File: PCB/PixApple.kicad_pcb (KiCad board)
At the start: 2 copper layers, 97.5 x 70 mm, 80 parts, among them J1 USB_C_Receptacle_USB2.0_16P, J10 Conn_01x11, J11 Conn_01x11, J12 Conn_01x02_Pin, J2 Conn_01x02_Pin, J28 Conn_01x01_Pin, J29 Conn_01x01_Pin, J3 Conn_01x01_Pin, J30 Conn_01x01_Pin, J4 Conn_01x01_Pin, J5 Conn_01x05_Pin, J6 Conn_01x02_Pin, J7 Conn_01x01_Pin, J8 Conn_02x03_Odd_Even, J9 Conn_01x04_Pin, M3 MountingHole_3.2mm_M3, SW1 SW_Push, SW2 SW_Push, U1 RP2040, U2 NCP1117-3.3_TO252, U3 W25Q128JVS, U4 SN65HVD230DR, U5 MCP2515-xSO, Y1 ABM8-272-T3, Y2 ABM8-16.000MHZ-B2-T

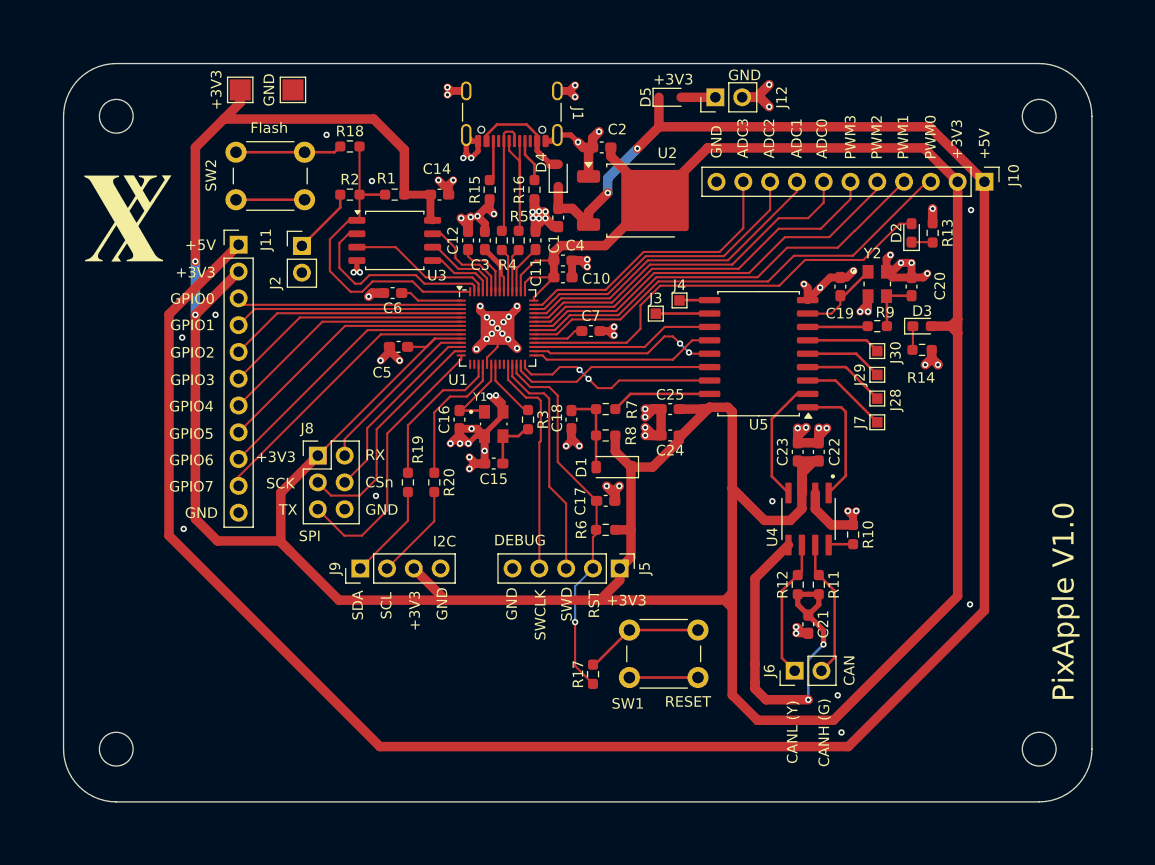
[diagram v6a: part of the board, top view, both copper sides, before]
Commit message: Fix pullup, connected 3V3 completely
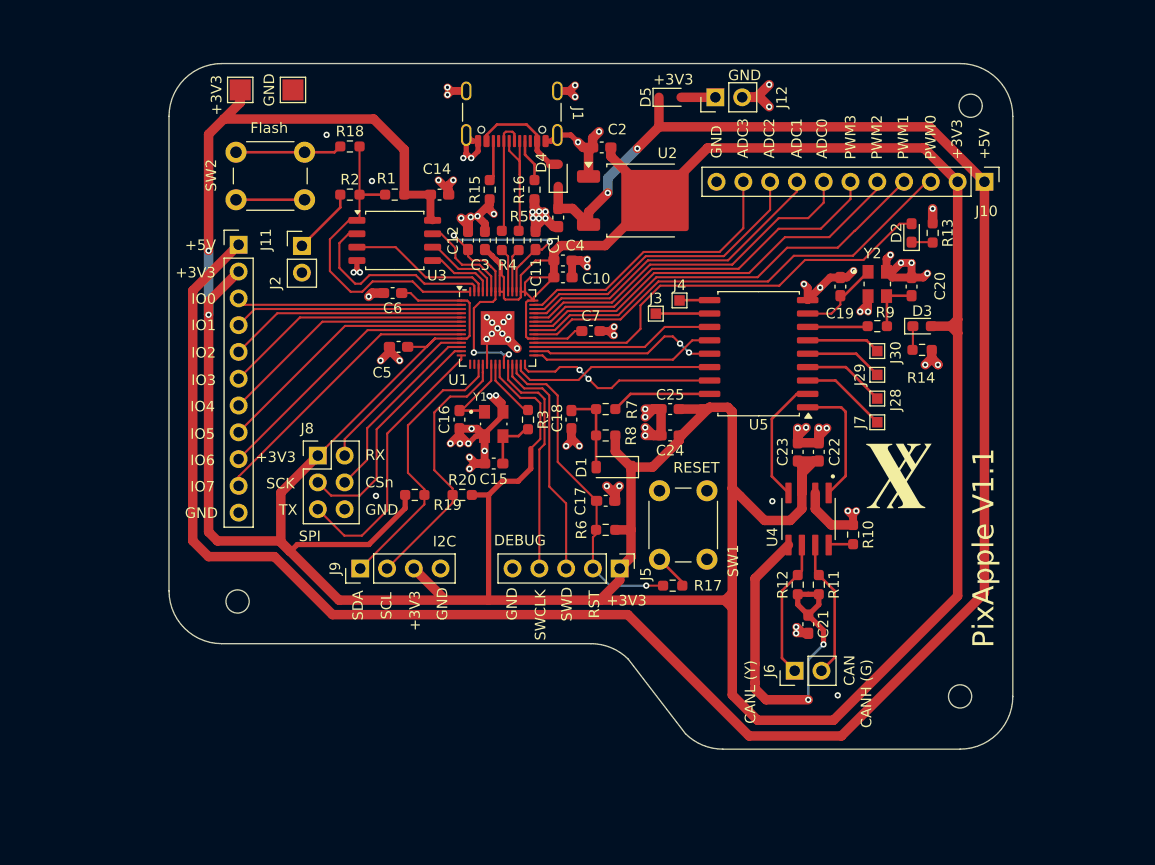
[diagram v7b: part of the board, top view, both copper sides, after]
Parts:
- removed M3 (x4): MountingHole_3.2mm_M3, MountingHole:MountingHole_3.2mm_M3
- added REF**: MountingHole_2.2mm_M2, MountingHole:MountingHole_2.2mm_M2, F.Cu at (129.0, 81.0)
- added REF**: MountingHole_2.2mm_M2, MountingHole:MountingHole_2.2mm_M2, F.Cu at (198.5, 34.0)
- added REF**: MountingHole_2.2mm_M2, MountingHole:MountingHole_2.2mm_M2, F.Cu at (197.5, 90.0)
- moved G*** 77.1 mm to (191.6, 69.0)
- moved SW1 17.7 mm to (173.5, 70.5), turned to -90 degrees
- moved R17 11.3 mm to (170.2, 79.5), turned to 180 degrees
- moved G*** 6.06 mm to (186.7, 72.2)
- moved R20 2.91 mm to (150.3, 70.9), turned to 0 degrees
- moved R19 1.36 mm to (145.8, 70.9), turned to 180 degrees
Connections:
- R19 pad 1: Net-(U1-GPIO14) -> /I2C1_SDA
- R19 pad 2: /I2C1_SDA -> +3V3
- R20 pad 1: Net-(U1-GPIO15) -> /I2C1_SCL
- R20 pad 2: /I2C1_SCL -> +3V3
- U1 pad 17: Net-(U1-GPIO14) -> /I2C1_SDA
- U1 pad 18: Net-(U1-GPIO15) -> /I2C1_SCL
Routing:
- net +3V3: track 399.5 -> 455.7 mm
- net +1V1: track 10.5 -> 35.4 mm, vias 0 -> 4
- net /I2C1_SDA: track 9.12 -> 26.5 mm
- net /I2C1_SCL: track 9.11 -> 25.5 mm
- net Net-(U1-GPIO14): track 14.3 -> 0.00 mm
- net Net-(U1-GPIO15): track 13.1 -> 0.00 mm
- net GND: track 172.7 -> 160.7 mm, vias 92 -> 83
- net Net-(R17-Pad1): track 11.3 -> 3.40 mm
- net /RESET: track 36.0 -> 31.0 mm
- net VBUS: track 215.3 -> 210.6 mm
- net /SWCLK: track 21.3 -> 21.9 mm
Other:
- board size 97.5 x 70 mm -> 80 x 65 mm
- board text added: "IO0"
- board text added: "IO1"
- board text added: "IO2"
- board text added: "IO3"
- board text added: "IO4"
- board text added: "IO5"
- board text added: "IO6"
- board text added: "IO7"
- board text added: "PixApple V1.1"
- board text removed: "GPIO0"
- board text removed: "GPIO1"
- board text removed: "GPIO2"
- board text removed: "GPIO3"
- board text removed: "GPIO4"
- board text removed: "GPIO5"
- board text removed: "GPIO6"
- board text removed: "GPIO7"

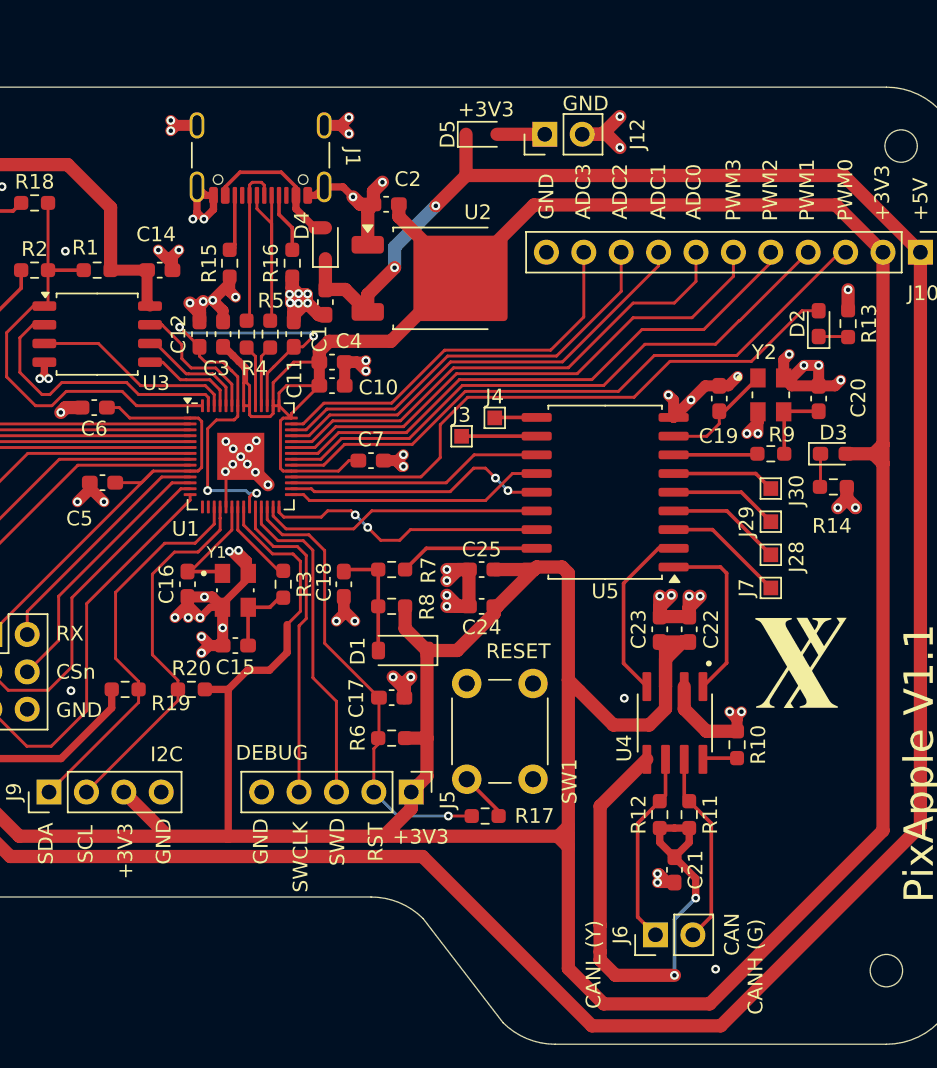
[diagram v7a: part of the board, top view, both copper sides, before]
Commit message: esd, pullup, error fix
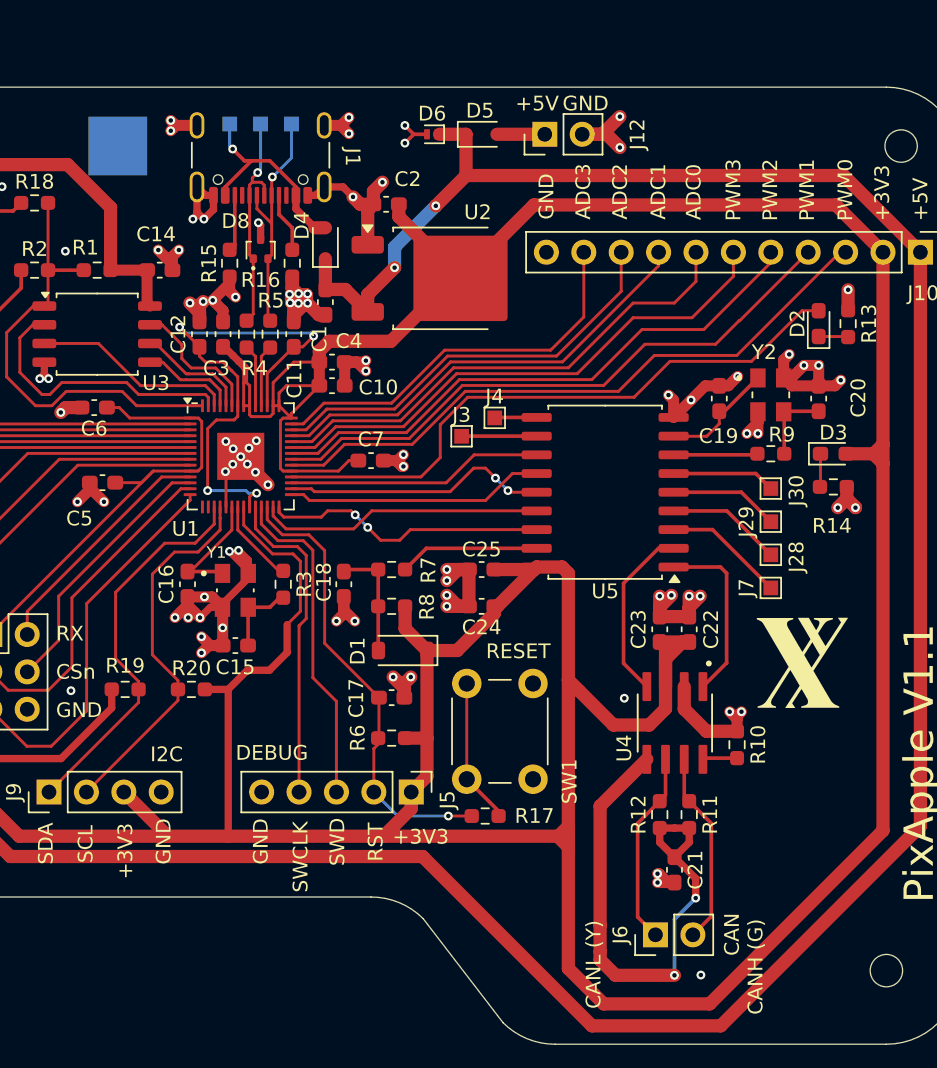
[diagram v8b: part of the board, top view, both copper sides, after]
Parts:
- added D6: PESD5V0S1UL, Diode_SMD:D_SOD-882, F.Cu at (166.7, 33.2)
- added D8: RCLAMP0502B, Package_TO_SOT_SMD:SOT-416, F.Cu at (155.0, 41.0)
- added REF**: TestPoint_Pad_1.0x1.0mm, TestPoint:TestPoint_Pad_1.0x1.0mm, B.Cu at (155.0, 32.5)
- added REF**: TestPoint_Pad_1.0x1.0mm, TestPoint:TestPoint_Pad_1.0x1.0mm, B.Cu at (157.1, 32.5)
- added REF**: TestPoint_Pad_1.0x1.0mm, TestPoint:TestPoint_Pad_1.0x1.0mm, B.Cu at (152.9, 32.5)
- added REF**: TestPoint_Pad_4.0x4.0mm, TestPoint:TestPoint_Pad_4.0x4.0mm, B.Cu at (145.3, 34.0)
- moved G*** 0.10 mm to (191.7, 69.0)
- turned R19 to 0 degrees
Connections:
- R19 pad 1: /I2C1_SDA -> +3V3
- R19 pad 2: +3V3 -> /I2C1_SDA
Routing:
- net Net-(R17-Pad1): track 3.40 -> 9.90 mm
- net /usb/USB_D-: track 12.2 -> 16.5 mm, vias 0 -> 1
- net Net-(D4-A): track 10.2 -> 14.3 mm, vias 0 -> 1
- net /usb/USB_D+: track 11.6 -> 15.6 mm, vias 0 -> 1
- net GND: track 160.7 -> 164.5 mm, vias 83 -> 86
- net VBUS: track 210.6 -> 212.4 mm
